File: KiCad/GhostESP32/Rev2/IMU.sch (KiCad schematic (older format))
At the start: 7 parts, among them U5 MPU-6050, U6 HMC5883

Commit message: Working on the Encoder
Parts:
- removed C4: 0.1uF, Capacitors_SMD:C_0603, symbol C
- removed C5: 10nF, Capacitors_SMD:C_0603, symbol C
- removed C6: 2.2nF, Capacitors_SMD:C_0603, symbol C
- removed C7: 0.22uF, Capacitors_SMD:C_0603, symbol C
- removed C8: 4.7uF, Capacitors_SMD:C_0603, symbol C
- added C11: 0.1uF, Capacitors_SMD:C_0603, symbol C
- added C12: 10nF, Capacitors_SMD:C_0603, symbol C
- added C13: 2.2nF, Capacitors_SMD:C_0603, symbol C
- added C14: 0.22uF, Capacitors_SMD:C_0603, symbol C
- added C15: 4.7uF, Capacitors_SMD:C_0603, symbol C
- U6: footprint NorBotKiCadFootprints:HMC5883 -> Housings_DFN_QFN:QFN-16-1EP_3x3mm_Pitch0.5mm
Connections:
- net GND: now also C11.1, C12.1, C13.1, C15.1
- net VCC: now also C12.2
- net at U5.10 (REGOUT): now also C11.2
- net at U5.20 (CPOUT): now also C13.2
- net at U6.10 (C1): now also C15.2
- net at U6.12 (SETC): now also C14.1
- net at U6.8 (SETP): now also C14.2
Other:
- note added: "MPU-6050 (Farnell: 186474, QFN-24)\nI2C address: 0x68 / 0x69 (depends on AD0 low or high)"
- note removed: "HMC5883 compass\nFarnell no: 197-1743\nI2C address: 0x1E"
- note removed: "MPU-6050 gyro/accelerometer\nFarnellno: 186-474\nFootprint: QFN-24\nI2C address: 0x68 / 0x69 (depends on AD0 low or high)"
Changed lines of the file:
@@
 EESchema Schematic File Version 2
-LIBS:GhostSensorboard-rescue
 LIBS:power
 LIBS:device
@@
 LIBS:NorBot
 LIBS:switches
-LIBS:GhostSensorboard-cache
+LIBS:GhostESP32-cache
 EELAYER 26 0
 EELAYER END
 $Descr A4 11693 8268
 encoding utf-8
-Sheet 2 3
-Title "Ghost Sensorboard"
-Date "2017-03-10"
-Rev "2"
-Comp "Frode Lillerud"
+Sheet 2 2
+Title ""
+Date ""
+Rev ""
+Comp ""
 Comment1 ""
 Comment2 ""
@@
 Comment4 ""
 $EndDescr
-Text Notes 2900 2750 0    60   ~ 0
-MPU-6050 gyro/accelerometer\nFarnellno: 186-474\nFootprint: QFN-24\nI2C address: 0x68 / 0x69 (depends on AD0 low or high)
+Text Notes 2700 2150 0    60   ~ 0
+MPU-6050 (Farnell: 186474, QFN-24)\nI2C address: 0x68 / 0x69 (depends on AD0 low or high)
 Text HLabel 2000 3400 0    60   Input ~ 0
 VCC
 $Comp
-L C C5
-U 1 1 574C3CF5
+L C C12
+U 1 1 58C9D2F8
 P 2400 3100
-F 0 "C5" H 2425 3200 50  0000 L CNN
+F 0 "C12" H 2425 3200 50  0000 L CNN
 F 1 "10nF" H 2425 3000 50  0000 L CNN
 F 2 "Capacitors_SMD:C_0603" H 2438 2950 50  0001 C CNN
@@
 $EndComp
 $Comp
-L GND #PWR051
-U 1 1 574C3F70
+L GND #PWR049
+U 1 1 58C9D2F9
 P 2400 2850
-F 0 "#PWR051" H 2400 2600 50  0001 C CNN
+F 0 "#PWR049" H 2400 2600 50  0001 C CNN
 F 1 "GND" H 2400 2700 50  0000 C CNN
 F 2 "" H 2400 2850 50  0000 C CNN
@@
 FSYNC
 $Comp
-L GND #PWR052
-U 1 1 574C4065
+L GND #PWR050
+U 1 1 58C9D2FA
 P 2700 3850
-F 0 "#PWR052" H 2700 3600 50  0001 C CNN
+F 0 "#PWR050" H 2700 3600 50  0001 C CNN
 F 1 "GND" H 2700 3700 50  0000 C CNN
 F 2 "" H 2700 3850 50  0000 C CNN
@@
 $EndComp
 $Comp
-L GND #PWR053
-U 1 1 574C40EB
+L GND #PWR051
+U 1 1 58C9D2FB
 P 2800 4750
-F 0 "#PWR053" H 2800 4500 50  0001 C CNN
+F 0 "#PWR051" H 2800 4500 50  0001 C CNN
 F 1 "GND" H 2800 4600 50  0000 C CNN
 F 2 "" H 2800 4750 50  0000 C CNN
@@
 GND
 $Comp
-L C C4
-U 1 1 574C41F0
+L C C11
+U 1 1 58C9D2FC
 P 2150 4300
-F 0 "C4" H 2175 4400 50  0000 L CNN
+F 0 "C11" H 2175 4400 50  0000 L CNN
 F 1 "0.1uF" H 2175 4200 50  0000 L CNN
 F 2 "Capacitors_SMD:C_0603" H 2188 4150 50  0001 C CNN
@@
 $EndComp
 $Comp
-L C C6
-U 1 1 574C457F
+L C C13
+U 1 1 58C9D2FD
 P 2450 4300
-F 0 "C6" H 2475 4400 50  0000 L CNN
+F 0 "C13" H 2475 4400 50  0000 L CNN
 F 1 "2.2nF" H 2475 4200 50  0000 L CNN
 F 2 "Capacitors_SMD:C_0603" H 2488 4150 50  0001 C CNN
@@
 $EndComp
 $Comp
-L GND #PWR054
-U 1 1 574C4E5A
+L GND #PWR052
+U 1 1 58C9D2FE
 P 4250 4000
-F 0 "#PWR054" H 4250 3750 50  0001 C CNN
+F 0 "#PWR052" H 4250 3750 50  0001 C CNN
 F 1 "GND" H 4250 3850 50  0000 C CNN
 F 2 "" H 4250 4000 50  0000 C CNN
@@
 $Comp
 L HMC5883 U6
-U 1 1 574C57C9
+U 1 1 58C9D2FF
 P 7500 3750
 F 0 "U6" H 8000 3050 60  0000 C CNN
 F 1 "HMC5883" H 7500 3750 60  0000 C CNN
-F 2 "NorBotKiCadFootprints:HMC5883" H 7500 3750 60  0001 C CNN
+F 2 "Housings_DFN_QFN:QFN-16-1EP_3x3mm_Pitch0.5mm" H 7500 3750 60  0001 C CNN
 F 3 "" H 7500 3750 60  0000 C CNN
 	1    7500 3750
@@
 VCC
 $Comp
-L C C7
-U 1 1 574C6C91
+L C C14
+U 1 1 58C9D300
 P 7800 5000
-F 0 "C7" H 7825 5100 50  0000 L CNN
+F 0 "C14" H 7825 5100 50  0000 L CNN
 F 1 "0.22uF" H 7825 4900 50  0000 L CNN
 F 2 "Capacitors_SMD:C_0603" H 7838 4850 50  0001 C CNN
@@
 $EndComp
 $Comp
-L GND #PWR055
-U 1 1 574C70FE
+L GND #PWR053
+U 1 1 58C9D301
 P 9450 4350
-F 0 "#PWR055" H 9450 4100 50  0001 C CNN
+F 0 "#PWR053" H 9450 4100 50  0001 C CNN
 F 1 "GND" H 9450 4200 50  0000 C CNN
 F 2 "" H 9450 4350 50  0000 C CNN
@@
 $EndComp
 $Comp
-L C C8
-U 1 1 574C7189
+L C C15
+U 1 1 58C9D302
 P 8850 3850
-F 0 "C8" H 8875 3950 50  0000 L CNN
+F 0 "C15" H 8875 3950 50  0000 L CNN
 F 1 "4.7uF" H 8875 3750 50  0000 L CNN
 F 2 "Capacitors_SMD:C_0603" H 8888 3700 50  0001 C CNN
@@
 $Comp
 L MPU-6050 U5
-U 1 1 574CEE9E
+U 1 1 58C9D303
 P 3450 3900
 F 0 "U5" H 3450 3450 60  0000 C CNN
@@
 Wire Wire Line
 	9850 5400 7800 5400
-Text Notes 8550 2800 0    60   ~ 0
-HMC5883 compass\nFarnell no: 197-1743\nI2C address: 0x1E
+NoConn ~ 4100 3500
 NoConn ~ 4100 3400
-NoConn ~ 4100 3500
 Text HLabel 6450 3450 0    60   Input ~ 0
 SCL

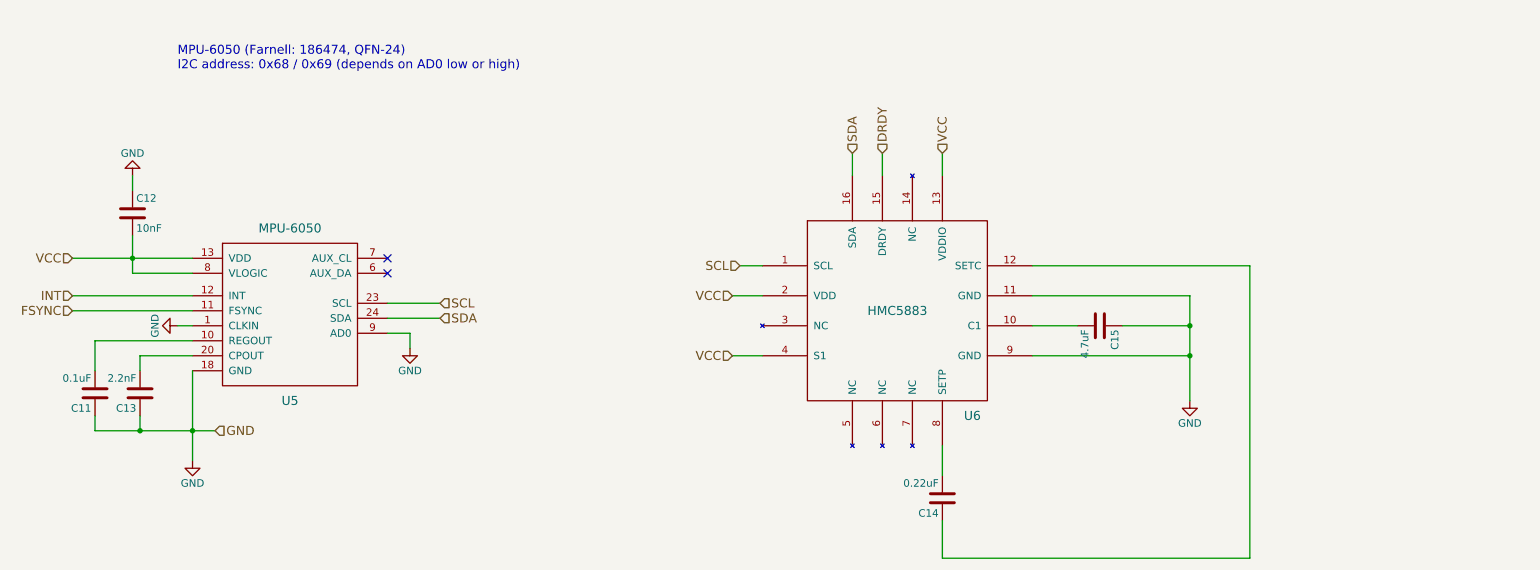
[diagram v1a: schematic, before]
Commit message: Ready to start routing. Schematics should be done.
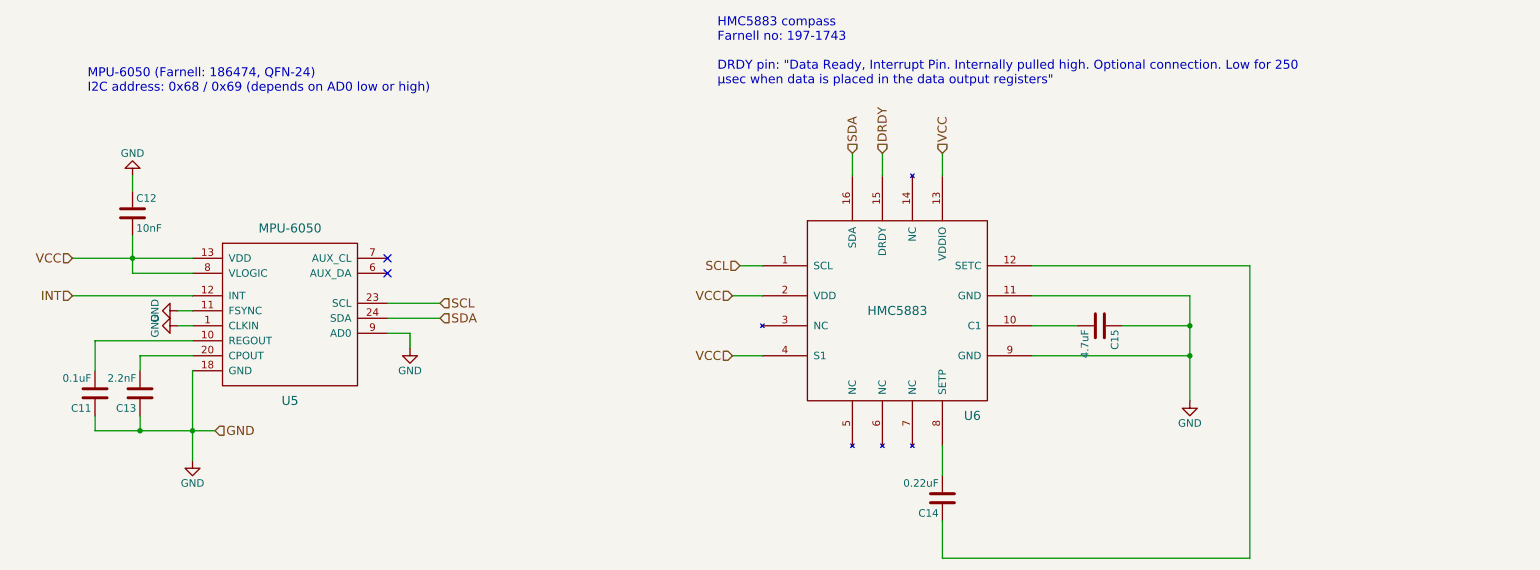
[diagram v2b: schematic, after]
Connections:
- net FSYNC is gone; now on net GND: U5.11 (FSYNC)
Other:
- note added: "HMC5883 compass\nFarnell no: 197-1743\n\nDRDY pin: "Data Ready, Interrupt Pin. Internally pulled high. Optional connection. Low for 250\nµsec when data is placed in the data output registers""
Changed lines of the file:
@@
 encoding utf-8
 Sheet 2 2
-Title ""
-Date ""
-Rev ""
-Comp ""
-Comment1 ""
+Title "Ghost ESP32"
+Date "2017-03-19"
+Rev "2"
+Comp "Frode Lillerud"
+Comment1 "Work in progress"
 Comment2 ""
 Comment3 ""
 Comment4 ""
 $EndDescr
-Text Notes 2700 2150 0    60   ~ 0
+Text Notes 2100 2300 0    60   ~ 0
 MPU-6050 (Farnell: 186474, QFN-24)\nI2C address: 0x68 / 0x69 (depends on AD0 low or high)
 Text HLabel 2000 3400 0    60   Input ~ 0
@@
 $EndComp
 $Comp
-L GND #PWR049
+L GND #PWR052
 U 1 1 58C9D2F9
 P 2400 2850
-F 0 "#PWR049" H 2400 2600 50  0001 C CNN
+F 0 "#PWR052" H 2400 2600 50  0001 C CNN
 F 1 "GND" H 2400 2700 50  0000 C CNN
 F 2 "" H 2400 2850 50  0000 C CNN
@@
 Text HLabel 2000 3650 0    60   Input ~ 0
 INT
-Text HLabel 2000 3750 0    60   Input ~ 0
-FSYNC
-$Comp
-L GND #PWR050
+$Comp
+L GND #PWR053
 U 1 1 58C9D2FA
 P 2700 3850
-F 0 "#PWR050" H 2700 3600 50  0001 C CNN
+F 0 "#PWR053" H 2700 3600 50  0001 C CNN
 F 1 "GND" H 2700 3700 50  0000 C CNN
 F 2 "" H 2700 3850 50  0000 C CNN
@@
 $EndComp
 $Comp
-L GND #PWR051
+L GND #PWR054
 U 1 1 58C9D2FB
 P 2800 4750
-F 0 "#PWR051" H 2800 4500 50  0001 C CNN
+F 0 "#PWR054" H 2800 4500 50  0001 C CNN
 F 1 "GND" H 2800 4600 50  0000 C CNN
 F 2 "" H 2800 4750 50  0000 C CNN
@@
 $EndComp
 $Comp
-L GND #PWR052
+L GND #PWR055
 U 1 1 58C9D2FE
 P 4250 4000
-F 0 "#PWR052" H 4250 3750 50  0001 C CNN
+F 0 "#PWR055" H 4250 3750 50  0001 C CNN
 F 1 "GND" H 4250 3850 50  0000 C CNN
 F 2 "" H 4250 4000 50  0000 C CNN
@@
 $EndComp
 $Comp
-L GND #PWR053
+L GND #PWR056
 U 1 1 58C9D301
 P 9450 4350
-F 0 "#PWR053" H 9450 4100 50  0001 C CNN
+F 0 "#PWR056" H 9450 4100 50  0001 C CNN
 F 1 "GND" H 9450 4200 50  0000 C CNN
 F 2 "" H 9450 4350 50  0000 C CNN
@@
 	2000 3650 2800 3650
 Wire Wire Line
-	2000 3750 2800 3750
+	2700 3750 2800 3750
 Wire Wire Line
 	2800 3850 2700 3850
@@
 	7800 5400 7800 5150
 Wire Wire Line
-	8400 4050 9450 4050
+	9450 4050 8400 4050
 Wire Wire Line
 	9450 3650 9450 4350
@@
 Text HLabel 7200 2700 1    60   Input ~ 0
 SDA
+$Comp
+L GND #PWR057
+U 1 1 58CD4E8D
+P 2700 3750
+F 0 "#PWR057" H 2700 3500 50  0001 C CNN
+F 1 "GND" H 2700 3600 50  0000 C CNN
+F 2 "" H 2700 3750 50  0000 C CNN
+F 3 "" H 2700 3750 50  0000 C CNN
+	1    2700 3750
+	0    1    1    0
+$EndComp
+Text Notes 6300 2250 0    60   ~ 0
+HMC5883 compass\nFarnell no: 197-1743\n\nDRDY pin: "Data Ready, Interrupt Pin. Internally pulled high. Optional connection. Low for 250\nµsec when data is placed in the data output registers"
 $EndSCHEMATC

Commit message: Minor
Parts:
- C11, C12, C13, C14, C15: symbol C -> GhostESP32-rescue:C-RESCUE-GhostESP32
- U5: symbol MPU-6050 -> NorBot:MPU-6050
- U6: symbol HMC5883 -> NorBot:HMC5883
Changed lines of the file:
@@
-EESchema Schematic File Version 2
-LIBS:power
-LIBS:device
-LIBS:transistors
-LIBS:conn
-LIBS:linear
-LIBS:regul
-LIBS:74xx
-LIBS:cmos4000
-LIBS:adc-dac
-LIBS:memory
-LIBS:xilinx
-LIBS:microcontrollers
-LIBS:dsp
-LIBS:microchip
-LIBS:analog_switches
-LIBS:motorola
-LIBS:texas
-LIBS:intel
-LIBS:audio
-LIBS:interface
-LIBS:digital-audio
-LIBS:philips
-LIBS:display
-LIBS:cypress
-LIBS:siliconi
-LIBS:opto
-LIBS:atmel
-LIBS:contrib
-LIBS:valves
-LIBS:NorBot
-LIBS:switches
+EESchema Schematic File Version 4
 LIBS:GhostESP32-cache
 EELAYER 26 0
@@
 VCC
 $Comp
-L C C12
+L GhostESP32-rescue:C-RESCUE-GhostESP32 C12
 U 1 1 58C9D2F8
 P 2400 3100
@@
 $EndComp
 $Comp
-L GND #PWR052
+L GhostESP32-rescue:GND-RESCUE-GhostESP32 #PWR052
 U 1 1 58C9D2F9
 P 2400 2850
@@
 INT
 $Comp
-L GND #PWR053
+L GhostESP32-rescue:GND-RESCUE-GhostESP32 #PWR053
 U 1 1 58C9D2FA
 P 2700 3850
@@
 $EndComp
 $Comp
-L GND #PWR054
+L GhostESP32-rescue:GND-RESCUE-GhostESP32 #PWR054
 U 1 1 58C9D2FB
 P 2800 4750
@@
 GND
 $Comp
-L C C11
+L GhostESP32-rescue:C-RESCUE-GhostESP32 C11
 U 1 1 58C9D2FC
 P 2150 4300
@@
 $EndComp
 $Comp
-L C C13
+L GhostESP32-rescue:C-RESCUE-GhostESP32 C13
 U 1 1 58C9D2FD
 P 2450 4300
@@
 $EndComp
 $Comp
-L GND #PWR055
+L GhostESP32-rescue:GND-RESCUE-GhostESP32 #PWR055
 U 1 1 58C9D2FE
 P 4250 4000
@@
 $EndComp
 $Comp
-L HMC5883 U6
+L NorBot:HMC5883 U6
 U 1 1 58C9D2FF
 P 7500 3750
@@
 VCC
 $Comp
-L C C14
+L GhostESP32-rescue:C-RESCUE-GhostESP32 C14
 U 1 1 58C9D300
 P 7800 5000
@@
 $EndComp
 $Comp
-L GND #PWR056
+L GhostESP32-rescue:GND-RESCUE-GhostESP32 #PWR056
 U 1 1 58C9D301
 P 9450 4350
@@
 $EndComp
 $Comp
-L C C15
+L GhostESP32-rescue:C-RESCUE-GhostESP32 C15
 U 1 1 58C9D302
 P 8850 3850
@@
 	7800 2850 7800 2700
 $Comp
-L MPU-6050 U5
+L NorBot:MPU-6050 U5
 U 1 1 58C9D303
 P 3450 3900
@@
 SDA
 $Comp
-L GND #PWR057
+L GhostESP32-rescue:GND-RESCUE-GhostESP32 #PWR057
 U 1 1 58CD4E8D
 P 2700 3750
